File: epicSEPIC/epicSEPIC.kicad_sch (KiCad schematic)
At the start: 13 parts, among them J1 Screw_Terminal_01x02, J2 Screw_Terminal_01x02, Q1 ISZ230N10NM6, U1 1EDN7550U

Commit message: PCB prototipo mejorado
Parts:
- added C4: 0.22u, Capacitor_SMD:C_0603_1608Metric, symbol Device:C
- added C5: 0.1u, Capacitor_SMD:C_0603_1608Metric, symbol Device:C
- added U2: LM7815, Package_TO_SOT_SMD:SOT-223-3_TabPin2, symbol Regulator_Linear:LM7815_TO220
- L1: footprint (none) -> Transformer_THT:Transformer_Toroid_Horizontal_D10.5mm_Amidon-T37
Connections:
- net GND: now also C4.2, C5.2, U2.2 (GND)
- net VDD: now also C5.1, U2.3 (VO)
- net input renamed +24V
- net +24V: now also C4.1, U2.1 (VI)

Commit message: PCB Final en proceso, encontré el inductor
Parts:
- L1: footprint Transformer_THT:Transformer_Toroid_Horizontal_D10.5mm_Amidon-T37 -> footprints:SRF1280680M
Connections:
- net GND: now also L1.2; no longer L1.3
- net S_Drain: now also L1.3; no longer L1.2
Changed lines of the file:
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@@
 			)
 		)
-		(property "Footprint" "Transformer_THT:Transformer_Toroid_Horizontal_D10.5mm_Amidon-T37"
+		(property "Footprint" "footprints:SRF1280680M"
 			(at 102.87 115.57 0)
 			(effects
@@
 	)
 	(symbol
+		(lib_name "L_Coupled_1")
 		(lib_id "epicsepic:L_Coupled")
 		(at 68.58 105.41 0)
@@
 			)
 		)
-		(property "Footprint" "Transformer_THT:Transformer_Toroid_Horizontal_D10.5mm_Amidon-T37"
+		(property "Footprint" "footprints:SRF1280680M"
 			(at 68.58 105.41 0)
 			(effects

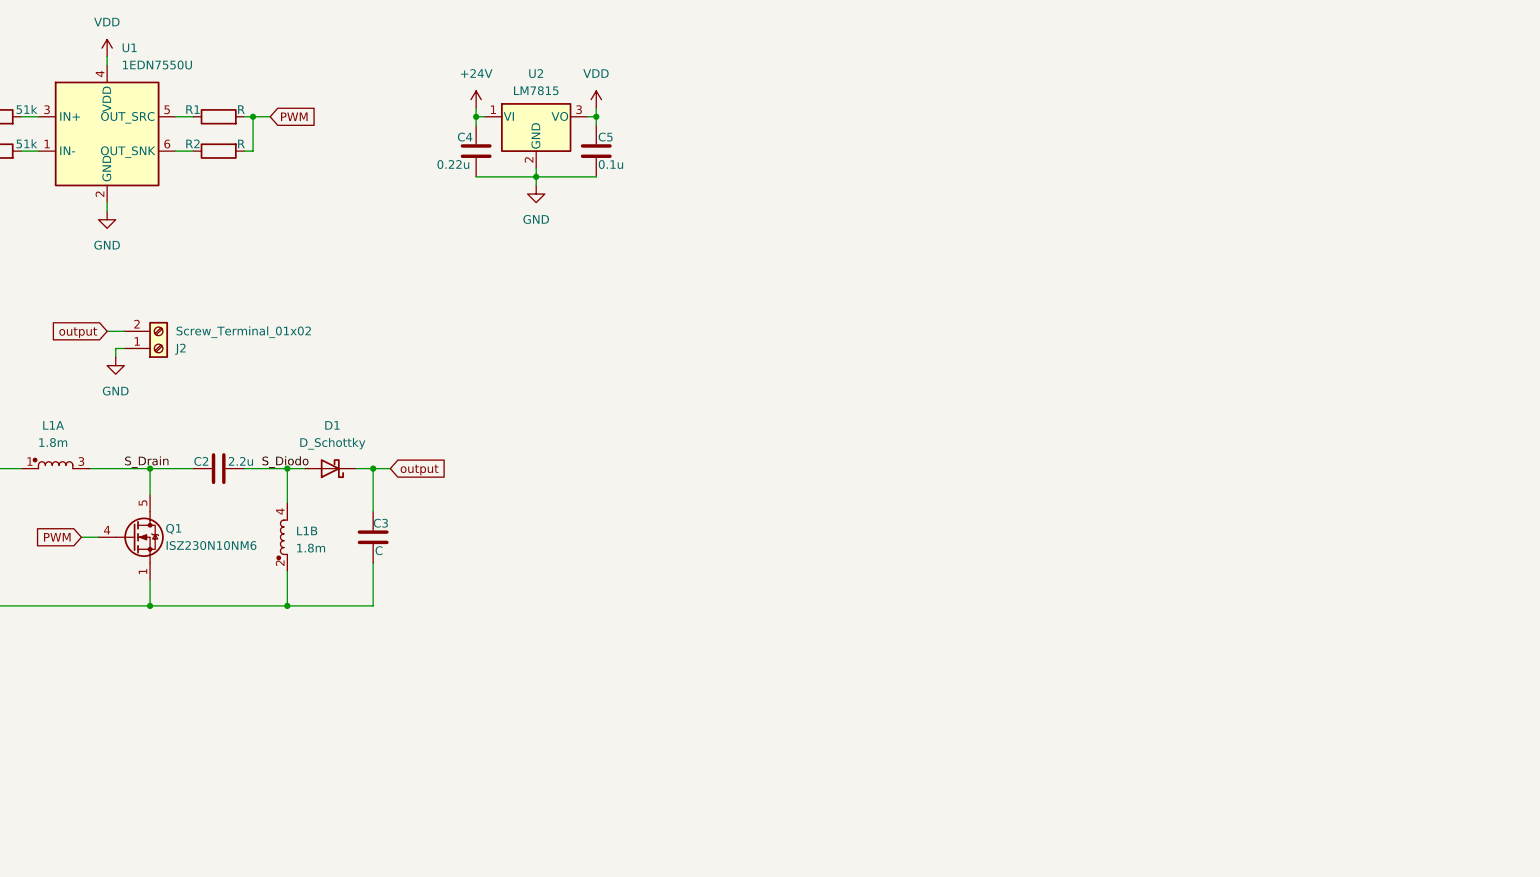
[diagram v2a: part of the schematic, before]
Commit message: Agregar repo submodulo para informe
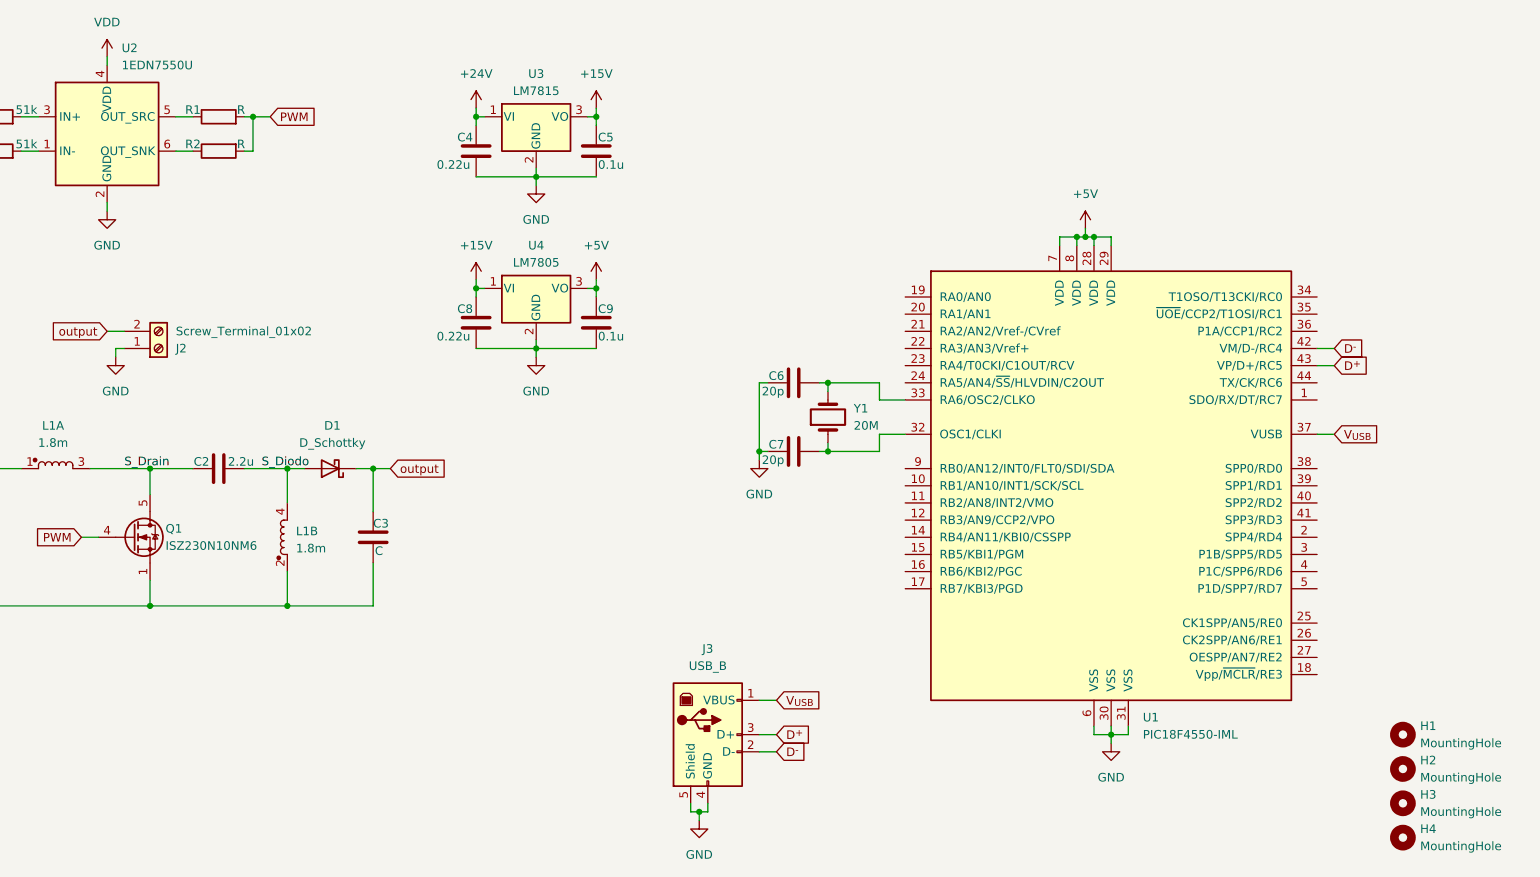
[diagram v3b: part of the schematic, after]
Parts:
- added C6, C7: 20p, symbol Device:C
- added C8: 0.22u, Capacitor_SMD:C_0603_1608Metric, symbol Device:C
- added C9: 0.1u, Capacitor_SMD:C_0603_1608Metric, symbol Device:C
- added H1, H2, H3, H4: MountingHole, MountingHole:MountingHole_3.2mm_M3_ISO14580, symbol Mechanical:MountingHole
- added J3: USB_B, symbol Connector:USB_B
- added U1: PIC18F4550-IML, Package_DFN_QFN:QFN-44-1EP_8x8mm_P0.65mm_EP6.45x6.45mm, symbol MCU_Microchip_PIC18:PIC18F4550-IML
- added U4: LM7805, Package_TO_SOT_THT:TO-220-3_Vertical, symbol Regulator_Linear:LM7805_TO220
- added Y1: 20M, symbol Device:Crystal
- renumbered U1 to U2, U2 to U3
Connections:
- net GND: now also C6.2, C7.1, C8.2, C9.2, J3.4 (GND), J3.5 (Shield), U1.30 (VSS), U1.31 (VSS), U1.6 (VSS), U4.2 (GND)
- net VDD: no longer C5.1, U3.3 (VO)
- new net: C7.2, U1.32 (OSC1/CLKI), Y1.1
- new net: C6.1, U1.33 (RA6/OSC2/CLKO), Y1.2
- new net +15V: C5.1, C8.1, U3.3 (VO), U4.1 (VI)
- new net +5V: C9.1, U1.28 (VDD), U1.29 (VDD), U1.7 (VDD), U1.8 (VDD), U4.3 (VO)
- new net D^{+}: J3.3 (D+), U1.43 (VP/D+/RC5)
- new net D^{-}: J3.2 (D-), U1.42 (VM/D-/RC4)
- new net V_{USB}: J3.1 (VBUS), U1.37 (VUSB)

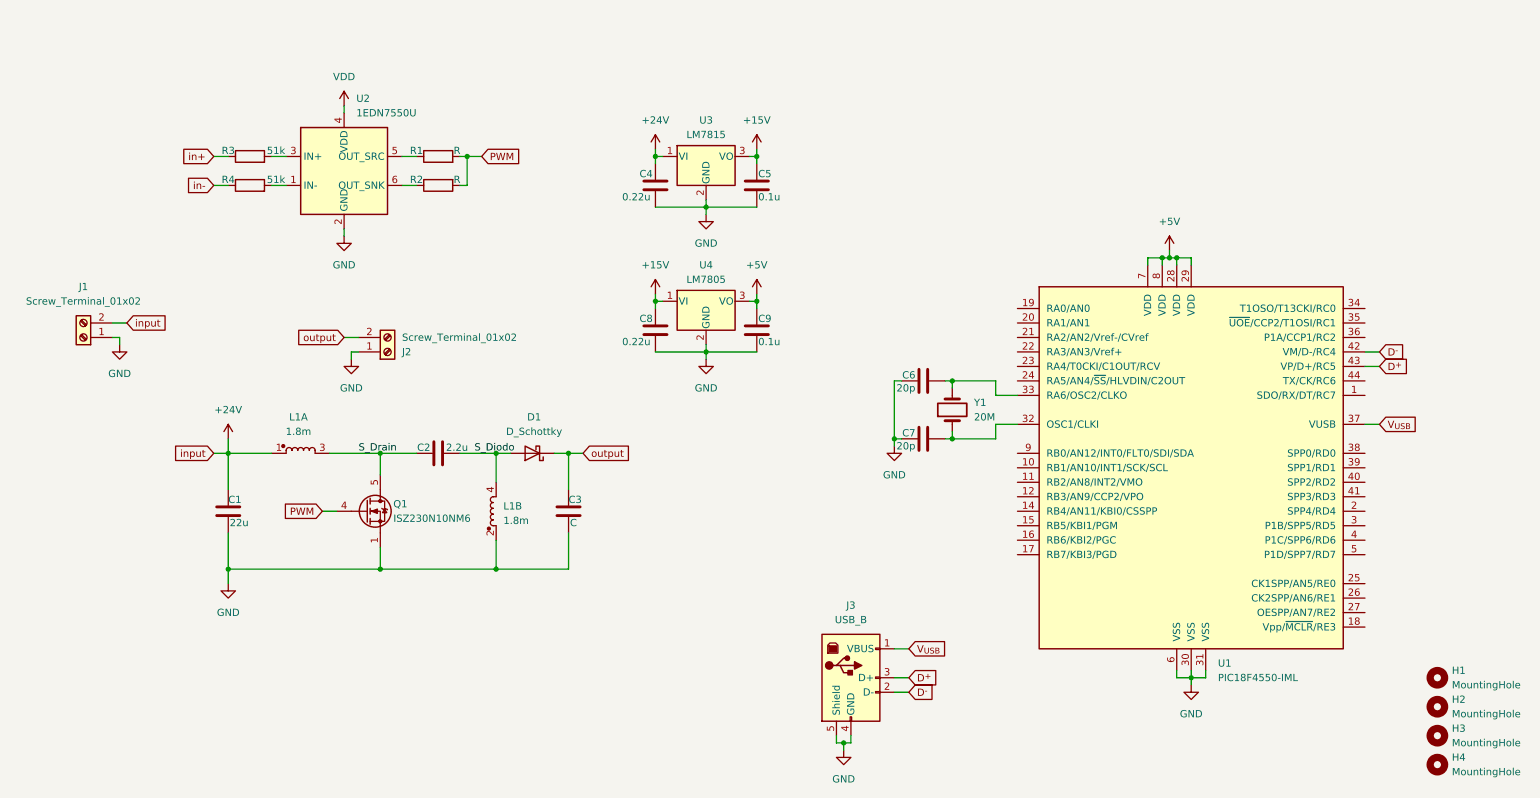
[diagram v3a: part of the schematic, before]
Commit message: Diseño de PCB final
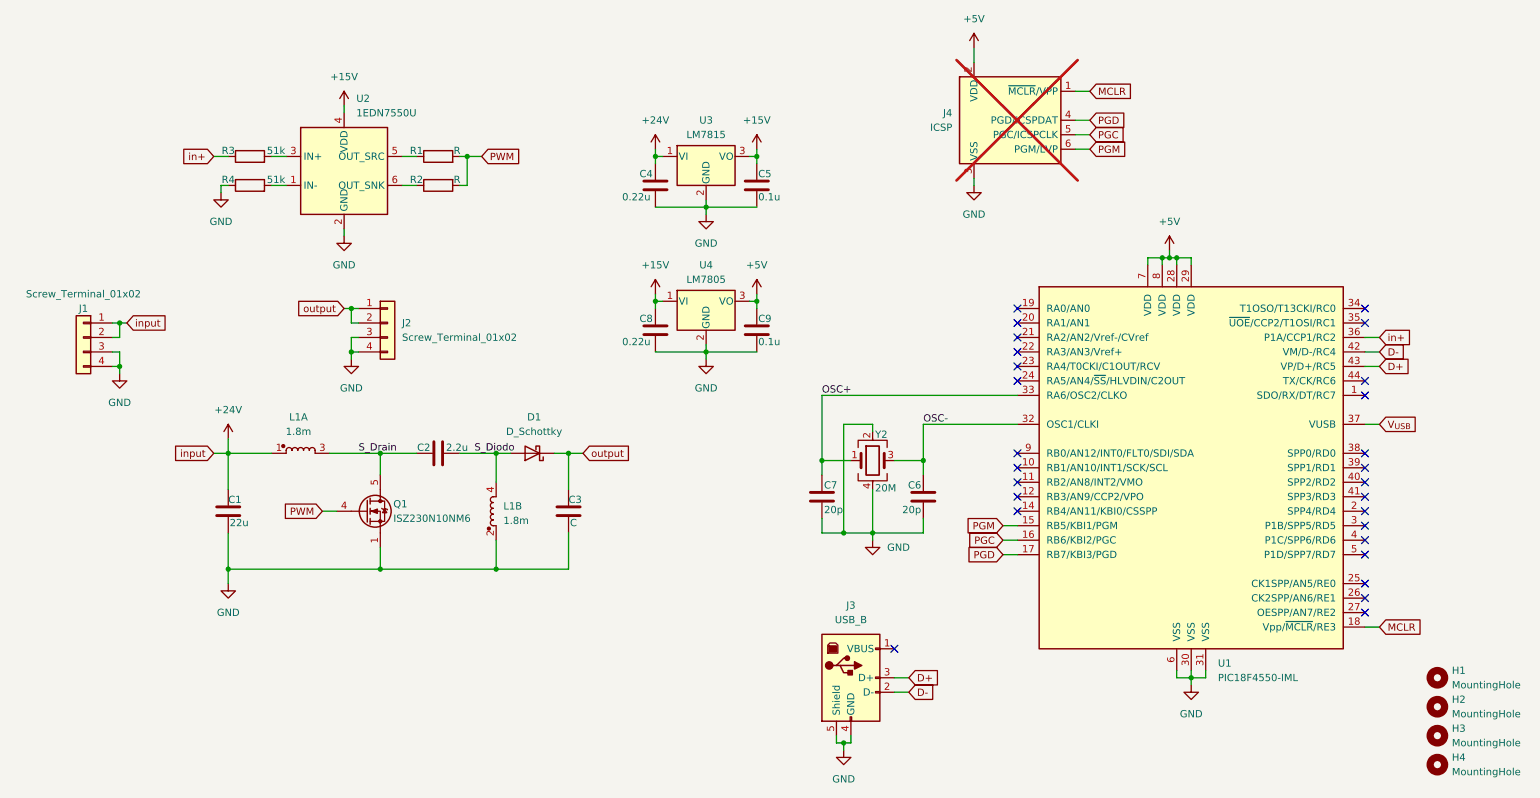
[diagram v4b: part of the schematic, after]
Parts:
- removed Y1: 20M, symbol Device:Crystal
- added J4: ICSP, Connector_PinSocket_1.00mm:PinSocket_1x06_P1.00mm_Vertical, symbol Connector:Conn_PIC_ICSP_ICD
- added Y2: 20M, Crystal:Crystal_SMD_2520-4Pin_2.5x2.0mm, symbol Device:Crystal_GND24
- C6, C7: footprint (none) -> Capacitor_SMD:C_0402_1005Metric
- J1, J2: footprint footprints:CONN2_2059-322&slash_998-403_WAG -> footprints:1822752; symbol Connector:Screw_Terminal_01x02 -> Connector_Generic:Conn_01x04
- J3: footprint (none) -> Connector_USB:USB_B_Lumberg_2411_02_Horizontal
- U4: footprint Package_TO_SOT_THT:TO-220-3_Vertical -> Package_TO_SOT_SMD:SOT-223-3_TabPin2
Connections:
- net VDD is gone; now on net +15V: U2.4 (VDD)
- net in- is gone; now on net GND: R4.1
- net +24V: now also J1.1 (Pin_1)
- net +5V: now also J4.2 (VDD)
- net GND: now also C6.1, C7.2, J1.3 (Pin_3), J1.4 (Pin_4), J2.3 (Pin_3), J2.4 (Pin_4), J4.3 (VSS), Y2.2, Y2.4; no longer C6.2, C7.1, J1.1 (Pin_1), J2.1 (Pin_1)
- net V_{USB}: no longer J3.1 (VBUS)
- net in+: now also U1.36 (P1A/CCP1/RC2)
- net output: now also J2.1 (Pin_1)
- net OSC-: now reaches U1.32 (OSC1/CLKI)
- net OSC-: now also C6.2, Y2.3; no longer C7.2
- net OSC+: now reaches U1.33 (RA6/OSC2/CLKO)
- net OSC+: now also C7.1, Y2.1; no longer C6.1
- net PGM: now reaches U1.15 (RB5/KBI1/PGM)
- net PGM: now also J4.6 (PGM/LVP)
- net PGC: now reaches U1.16 (RB6/KBI2/PGC)
- net PGC: now also J4.5 (PGC/ICSPCLK)
- net PGD: now reaches U1.17 (RB7/KBI3/PGD)
- net PGD: now also J4.4 (PGD/ICSPDAT)
- net MCLR: now reaches U1.18 (Vpp/~{MCLR}/RE3)
- net MCLR: now also J4.1 (~{MCLR}/VPP)
- net D^{+} renamed D+
- net D^{-} renamed D-
- no-connect marks 0 -> 27
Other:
- moved on the sheet: C6, C7

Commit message: PCB final
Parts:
- removed C1: 22u, Capacitor_SMD:C_Elec_4x5.8, symbol Device:C
- removed C2: 2.2u, Capacitor_SMD:C_0805_2012Metric, symbol Device:C
- removed C3: C, Capacitor_SMD:C_Elec_8x10.2, symbol Device:C
- removed C4, C8: 0.22u, Capacitor_SMD:C_0603_1608Metric, symbol Device:C
- removed C5, C9: 0.1u, Capacitor_SMD:C_0603_1608Metric, symbol Device:C
- removed C6, C7: 20p, Capacitor_SMD:C_0402_1005Metric, symbol Device:C
- removed D1: D_Schottky, Diode_SMD:D_SMB, symbol Device:D_Schottky
- removed J4: ICSP, Connector_PinSocket_1.00mm:PinSocket_1x06_P1.00mm_Vertical, symbol Connector:Conn_PIC_ICSP_ICD
- removed L1: 1.8m, footprints:SRF1280680M, symbol epicsepic:L_Coupled
- removed Q1: ISZ230N10NM6, footprints:PG-TSDSON-8-25, symbol epicsepic:ISZ230N10NM6
- removed R1, R2: R, Resistor_SMD:R_0402_1005Metric, symbol Device:R
- removed R3, R4: 51k, Resistor_SMD:R_0603_1608Metric, symbol Device:R
- removed U1: PIC18F4550-IML, Package_DFN_QFN:QFN-44-1EP_8x8mm_P0.65mm_EP6.45x6.45mm, symbol MCU_Microchip_PIC18:PIC18F4550-IML
- removed U2: 1EDN7550U, footprints:PG-TSNP-6-13, symbol epicsepic:1EDN7550U
- removed U3: LM7815, Package_TO_SOT_SMD:SOT-223-3_TabPin2, symbol Regulator_Linear:LM7815_TO220
- removed U4: LM7805, Package_TO_SOT_SMD:SOT-223-3_TabPin2, symbol Regulator_Linear:LM7805_TO220
- removed Y2: 20M, Crystal:Crystal_SMD_2520-4Pin_2.5x2.0mm, symbol Device:Crystal_GND24
- J1: value Screw_Terminal_01x02 -> Entrada 24V
- J2: renamed from J3; value USB_B -> USB Tipo B
- J3: renamed from J2; value Screw_Terminal_01x02 -> Salida 12-48V
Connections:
- net +24V renamed Potencia/Vin
- net D+ renamed Control/D+
- net D- renamed Control/D-
- net output renamed Potencia/Vout
- no-connect marks 27 -> 1
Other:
- added sheet Control (control.kicad_sch)
- added sheet Potencia (potencia.kicad_sch)
- added sheet Regulación (regulacion.kicad_sch)
- moved on the sheet: H1, H2, H3, H4, J1, J2, J3

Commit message: Agregar datasheets
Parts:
- J1, J3: Part Number (none) -> 1822752
- J2: Part Number (none) -> 61729-0010RLF
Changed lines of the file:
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@@
 			)
 		)
-		(property "Datasheet" "~"
+		(property "Datasheet" "https://cdn.amphenol-cs.com/media/wysiwyg/files/drawing/61729.pdf"
 			(at 120.65 80.01 0)
 			(effects
@@
 		)
 		(property "Description" "USB Type B connector"
+			(at 116.84 78.74 0)
+			(effects
+				(font
+					(size 1.27 1.27)
+				)
+				(hide yes)
+			)
+		)
+		(property "Part Number" "61729-0010RLF"
 			(at 116.84 78.74 0)
 			(effects
@@
 			)
 		)
-		(property "Datasheet" "~"
+		(property "Datasheet" "https://product-download.phoenixcontact.com/8109099?response-content-disposition=inline;%20filename%3D%221822752_07_en_03.pdf%22&Expires=1764883973&Signature=r3YrfBYqzjIP56~JDiCDsF6h9L-qF0WKHI2x2nMTL5bGgKmBSmGF-JVu5t~vrgeIWEqDLSKTApcxuj5AGaL7qxo9SfgojHmQFyjuf6W58z9cd60zgbMPpkCbU0Ujg9f9ZlDFkuhHVS7UxzlKDmhaI41QVOeZWDUMwJRgc47rVx0KIRGWLOXGG1wCKXEEU9wQd0mSrsloYGTRFyDHXxjxe7VbqXoXSbps2tSgRFvzxG3JsE8ME~~Gs4kVIeH8os7M4BhCt4iXYn3oeXkdkOsPUfEIaZRWc401pnOsAHUbwM4nOr4~n3NkdIglL26FD0NkNqj52azpdmjNtaxelcDWjQ__&Key-Pair-Id=K1I2N54A7B0GD"
 			(at 204.47 114.3 0)
 			(effects
@@
 		)
 		(property "Description" "Generic connector, single row, 01x04, script generated (kicad-library-utils/schlib/autogen/connector/)"
+			(at 204.47 114.3 0)
+			(effects
+				(font
+					(size 1.27 1.27)
+				)
+				(hide yes)
+			)
+		)
+		(property "Part Number" "1822752"
 			(at 204.47 114.3 0)
 			(effects
@@
 			)
 		)
-		(property "Datasheet" "~"
+		(property "Datasheet" "https://product-download.phoenixcontact.com/8109099?response-content-disposition=inline;%20filename%3D%221822752_07_en_03.pdf%22&Expires=1764883973&Signature=r3YrfBYqzjIP56~JDiCDsF6h9L-qF0WKHI2x2nMTL5bGgKmBSmGF-JVu5t~vrgeIWEqDLSKTApcxuj5AGaL7qxo9SfgojHmQFyjuf6W58z9cd60zgbMPpkCbU0Ujg9f9ZlDFkuhHVS7UxzlKDmhaI41QVOeZWDUMwJRgc47rVx0KIRGWLOXGG1wCKXEEU9wQd0mSrsloYGTRFyDHXxjxe7VbqXoXSbps2tSgRFvzxG3JsE8ME~~Gs4kVIeH8os7M4BhCt4iXYn3oeXkdkOsPUfEIaZRWc401pnOsAHUbwM4nOr4~n3NkdIglL26FD0NkNqj52azpdmjNtaxelcDWjQ__&Key-Pair-Id=K1I2N54A7B0GD"
 			(at 102.87 116.84 0)
 			(effects
@@
 			(at 102.87 116.84 0)
 			(effects
+				(font
+					(size 1.27 1.27)
+				)
+				(hide yes)
+			)
+		)
+		(property "Part Number" "1822752"
+			(at 102.87 116.84 0)
+			(effects

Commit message: PCB Final con reguladores
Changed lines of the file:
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@@
-	(wire
-		(pts
-			(xy 180.975 111.76) (xy 198.12 111.76)
-		)
-		(stroke
-			(width 0)
-			(type default)
-		)
-	)
 	(wire
 		(pts
@@
 	(wire
 		(pts
-			(xy 140.97 78.74) (xy 151.765 78.74)
+			(xy 180.34 111.76) (xy 198.12 111.76)
 		)
 		(stroke
@@
 	(wire
 		(pts
+			(xy 109.22 60.96) (xy 124.46 60.96)
+		)
+		(stroke
+			(width 0)
+			(type default)
+		)
+	)
+	(wire
+		(pts
 			(xy 124.46 81.28) (xy 138.43 81.28)
 		)
@@
 	(wire
 		(pts
+			(xy 140.97 78.74) (xy 151.13 78.74)
+		)
+		(stroke
+			(width 0)
+			(type default)
+		)
+	)
+	(wire
+		(pts
 			(xy 198.12 111.76) (xy 199.39 111.76)
 		)
@@
 	(wire
 		(pts
-			(xy 140.97 81.28) (xy 151.765 81.28)
-		)
-		(stroke
-			(width 0)
-			(type default)
-		)
-	)
-	(wire
-		(pts
 			(xy 115.57 90.17) (xy 116.84 90.17)
 		)
@@
 	(wire
 		(pts
-			(xy 125.095 60.96) (xy 109.22 60.96)
-		)
-		(stroke
-			(width 0)
-			(type default)
-		)
-	)
-	(wire
-		(pts
 			(xy 116.84 90.17) (xy 116.84 88.9)
 		)
@@
 		(pts
 			(xy 109.22 121.92) (xy 109.22 123.19)
+		)
+		(stroke
+			(width 0)
+			(type default)
+		)
+	)
+	(wire
+		(pts
+			(xy 140.97 81.28) (xy 151.13 81.28)
 		)
 		(stroke
@@
 			)
 		)
-		(property "Datasheet" "https://product-download.phoenixcontact.com/8109099?response-content-disposition=inline;%20filename%3D%221822752_07_en_03.pdf%22&Expires=1764883973&Signature=r3YrfBYqzjIP56~JDiCDsF6h9L-qF0WKHI2x2nMTL5bGgKmBSmGF-JVu5t~vrgeIWEqDLSKTApcxuj5AGaL7qxo9SfgojHmQFyjuf6W58z9cd60zgbMPpkCbU0Ujg9f9ZlDFkuhHVS7UxzlKDmhaI41QVOeZWDUMwJRgc47rVx0KIRGWLOXGG1wCKXEEU9wQd0mSrsloYGTRFyDHXxjxe7VbqXoXSbps2tSgRFvzxG3JsE8ME~~Gs4kVIeH8os7M4BhCt4iXYn3oeXkdkOsPUfEIaZRWc401pnOsAHUbwM4nOr4~n3NkdIglL26FD0NkNqj52azpdmjNtaxelcDWjQ__&Key-Pair-Id=K1I2N54A7B0GD"
+		(property "Datasheet" "~"
 			(at 102.87 116.84 0)
 			(effects
@@
 	)
 	(sheet
-		(at 151.765 69.85)
-		(size 12.7 19.05)
+		(at 151.13 69.85)
+		(size 13.335 19.05)
 		(exclude_from_sim no)
 		(in_bom yes)
@@
 		)
 		(property "Sheetname" "Control"
-			(at 158.496 90.932 0)
+			(at 157.861 90.932 0)
 			(effects
 				(font
@@
 		)
 		(property "Sheetfile" "control.kicad_sch"
-			(at 159.004 91.694 0)
+			(at 158.369 91.694 0)
 			(effects
 				(font
@@
 		)
 		(pin "D+" input
-			(at 151.765 81.28 180)
+			(at 151.13 81.28 180)
 			(effects
 				(font
@@
 		)
 		(pin "D-" input
-			(at 151.765 78.74 180)
+			(at 151.13 78.74 180)
 			(effects
 				(font
@@
 	)
 	(sheet
-		(at 125.095 55.88)
-		(size 18.415 10.16)
+		(at 124.46 55.88)
+		(size 19.05 10.16)
 		(exclude_from_sim no)
 		(in_bom yes)
@@
 		)
 		(property "Sheetname" "Regulación"
-			(at 125.095 55.1684 0)
+			(at 124.46 55.1684 0)
 			(effects
 				(font
@@
 		)
 		(property "Sheetfile" "regulacion.kicad_sch"
-			(at 125.095 66.6246 0)
+			(at 124.46 66.6246 0)
 			(effects
 				(font
@@
 		)
 		(pin "+24V" input
-			(at 125.095 60.96 180)
+			(at 124.46 60.96 180)
 			(effects
 				(font
@@
 	(sheet
 		(at 162.56 106.68)
-		(size 18.415 10.16)
+		(size 17.78 10.16)
 		(exclude_from_sim no)
 		(in_bom yes)
@@
 		)
 		(pin "Vout" input
-			(at 180.975 111.76 0)
-			(effects
-				(font
+			(at 180.34 111.76 0)
+			(effects
+				(font
